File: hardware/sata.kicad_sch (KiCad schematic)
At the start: 35 parts, among them IC1 ASM1061, J9 SATA_22pin, Q2 FDS4435BZ, Q3 FDS4435BZ, Q5 2N7002, Q6 2N7002, Y1 25MHz

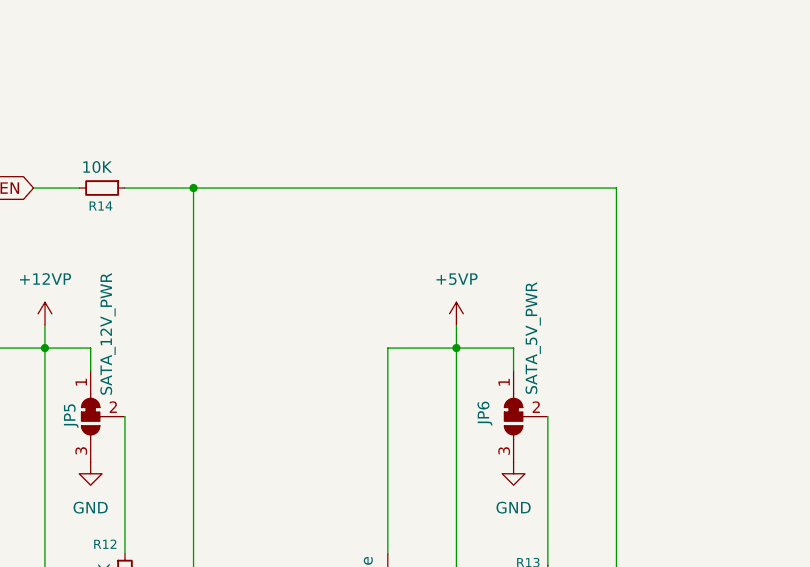
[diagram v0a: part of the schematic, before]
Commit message: feat: add R15 (100K) pull-down on SATA N-FET gate for boot safety
Ensures SATA power stays OFF during boot before GPIO5 is configured.
R15 pulls Net-(Q5-G) to GND. Normal operation unaffected (3.0V at gate
with GPIO5 high, well above 2N7002 threshold).
DRC: 0 errors, 1 cosmetic warning (Y1 silkscreen).
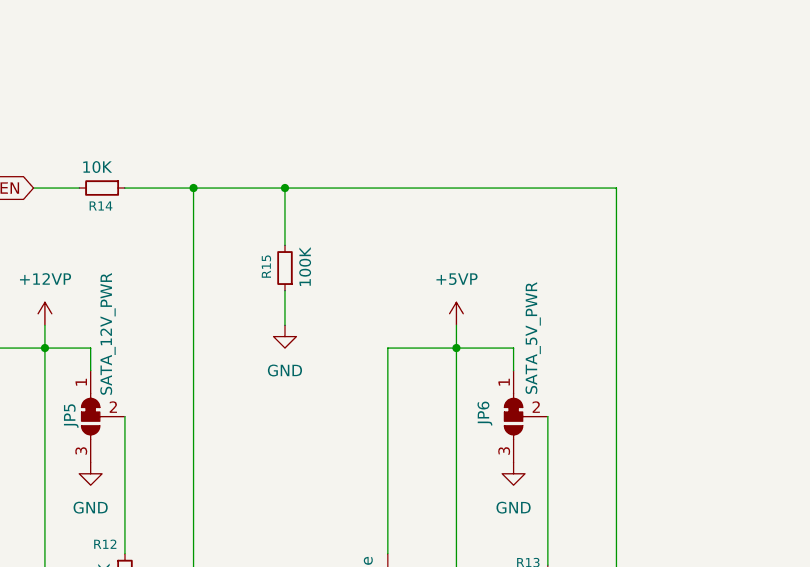
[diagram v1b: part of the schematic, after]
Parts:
- added R15: 100K, Resistor_SMD:R_0805_2012Metric, symbol Device:R_Small
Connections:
- net GND: now also R15.1
- net at Q5.1 (G), Q6.1 (G), R14.1: now also R15.2
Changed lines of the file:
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@@
 	)
 	(junction
+		(at 57.15 77.47)
+		(diameter 0)
+		(color 0 0 0 0)
+	)
+	(junction
 		(at 133.35 85.09)
 		(diameter 0)
@@
 	(wire
 		(pts
+			(xy 57.15 77.47) (xy 46.99 77.47)
+		)
+		(stroke
+			(width 0)
+			(type default)
+		)
+	)
+	(wire
+		(pts
 			(xy 39.37 102.87) (xy 39.37 118.11)
 		)
@@
 	(wire
 		(pts
-			(xy 93.98 77.47) (xy 46.99 77.47)
+			(xy 93.98 77.47) (xy 57.15 77.47)
 		)
 		(stroke
@@
 	(wire
 		(pts
+			(xy 57.15 77.47) (xy 57.15 83.82)
+		)
+		(stroke
+			(width 0)
+			(type default)
+		)
+	)
+	(wire
+		(pts
 			(xy 242.57 63.5) (xy 242.57 64.77)
 		)
@@
 		)
 	)
+	(wire
+		(pts
+			(xy 57.15 88.9) (xy 57.15 92.71)
+		)
+		(stroke
+			(width 0)
+			(type default)
+		)
+	)
 	(label "+12V_S"
 		(at 41.91 172.72 0)
@@
 	)
 	(symbol
+		(lib_id "power:GND")
+		(at 57.15 92.71 0)
+		(unit 1)
+		(body_style 1)
+		(exclude_from_sim no)
+		(in_bom yes)
+		(on_board yes)
+		(in_pos_files yes)
+		(dnp no)
+		(fields_autoplaced yes)
+		(property "Reference" "#PWR092"
+			(at 57.15 99.06 0)
+			(hide yes)
+			(show_name no)
+			(do_not_autoplace no)
+			(effects
+				(font
+					(size 1.27 1.27)
+				)
+			)
+		)
+		(property "Value" "GND"
+			(at 57.15 97.79 0)
+			(show_name no)
+			(do_not_autoplace no)
+			(effects
+				(font
+					(size 1.27 1.27)
+				)
+			)
+		)
+		(property "Footprint" ""
+			(at 57.15 92.71 0)
+			(hide yes)
+			(show_name no)
+			(do_not_autoplace no)
+			(effects
+				(font
+					(size 1.27 1.27)
+				)
+			)
+		)
+		(property "Datasheet" ""
+			(at 57.15 92.71 0)
+			(hide yes)
+			(show_name no)
+			(do_not_autoplace no)
+			(effects
+				(font
+					(size 1.27 1.27)
+				)
+			)
+		)
+		(property "Description" "Power symbol creates a global label with name \"GND\" , ground"
+			(at 57.15 92.71 0)
+			(hide yes)
+			(show_name no)
+			(do_not_autoplace no)
+			(effects
+				(font
+					(size 1.27 1.27)
+				)
+			)
+		)
+		(pin "1"
+		)
+		(instances
+			(project "granit"
+				(path "/d2c135e3-a983-4cd4-8cff-b50ca3c7671a/b486f39b-2401-4245-9dd6-e411236f99dc"
+					(reference "#PWR092")
+					(unit 1)
+				)
+			)
+		)
+	)
+	(symbol
 		(lib_id "Device:C_Small")
 		(at 177.8 133.35 0)
@@
 					(unit 1)
 				)
+			)
+		)
+	)
+	(symbol
+		(lib_id "Device:R_Small")
+		(at 57.15 86.36 180)
+		(unit 1)
+		(body_style 1)
+		(exclude_from_sim no)
+		(in_bom yes)
+		(on_board yes)
+		(in_pos_files yes)
+		(dnp no)
+		(property "Reference" "R15"
+			(at 55.118 84.836 90)
+			(show_name no)
+			(do_not_autoplace no)
+			(effects
+				(font
+					(size 1.016 1.016)
+				)
+				(justify left)
+			)
+		)
+		(property "Value" "100K"
+			(at 59.436 84.074 90)
+			(show_name no)
+			(do_not_autoplace no)
+			(effects
+				(font
+					(size 1.27 1.27)
+				)
+				(justify left)
+			)
+		)
+		(property "Footprint" "Resistor_SMD:R_0805_2012Metric"
+			(at 57.15 86.36 0)
+			(hide yes)
+			(show_name no)
+			(do_not_autoplace no)
+			(effects
+				(font
+					(size 1.27 1.27)
+				)
+			)
+		)
+		(property "Datasheet" ""
+			(at 57.15 86.36 0)
+			(hide yes)
+			(show_name no)
+			(do_not_autoplace no)
+			(effects
+				(font
+					(size 1.27 1.27)
+				)
+			)
+		)
+		(property "Description" "Resistor, small symbol"
+			(at 57.15 86.36 0)
+			(hide yes)
+			(show_name no)
+			(do_not_autoplace no)
+			(effects
+				(font
+					(size 1.27 1.27)
+				)
+			)
+		)
+		(pin "1"
+		)
+		(pin "2"
+		)
+		(instances
+			(project "granit"
+				(path "/d2c135e3-a983-4cd4-8cff-b50ca3c7671a/b486f39b-2401-4245-9dd6-e411236f99dc"
+					(reference "R15")
+					(unit 1)
+				)
